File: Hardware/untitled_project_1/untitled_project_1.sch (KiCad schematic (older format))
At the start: 1 part

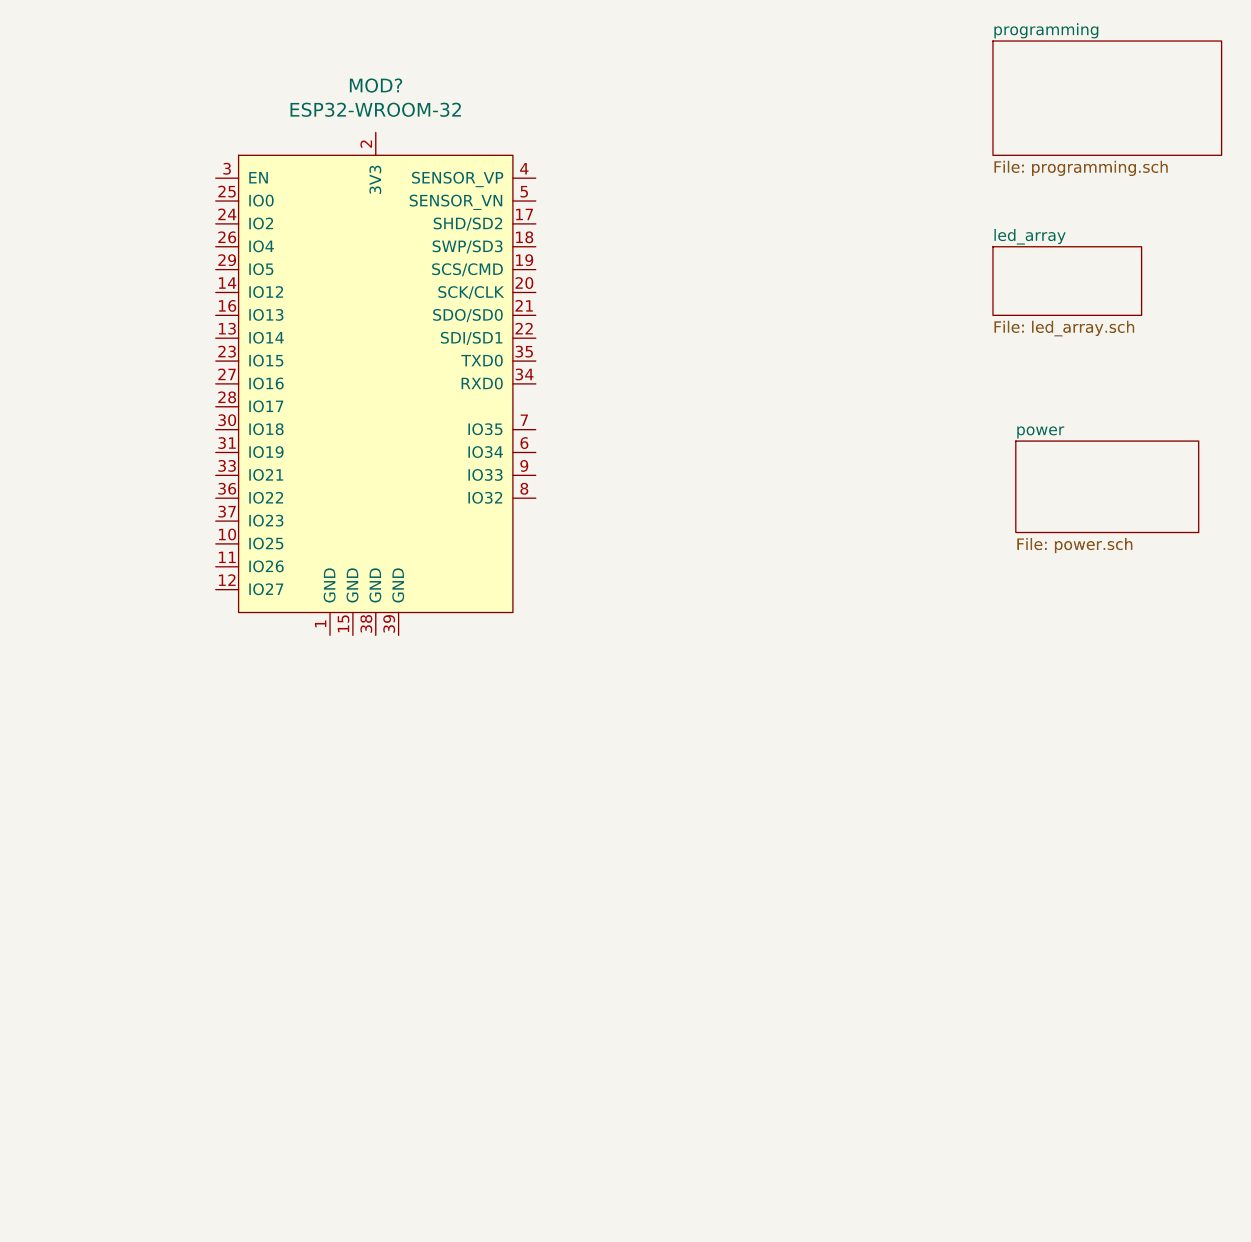
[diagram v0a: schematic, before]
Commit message: add power and programming schematics
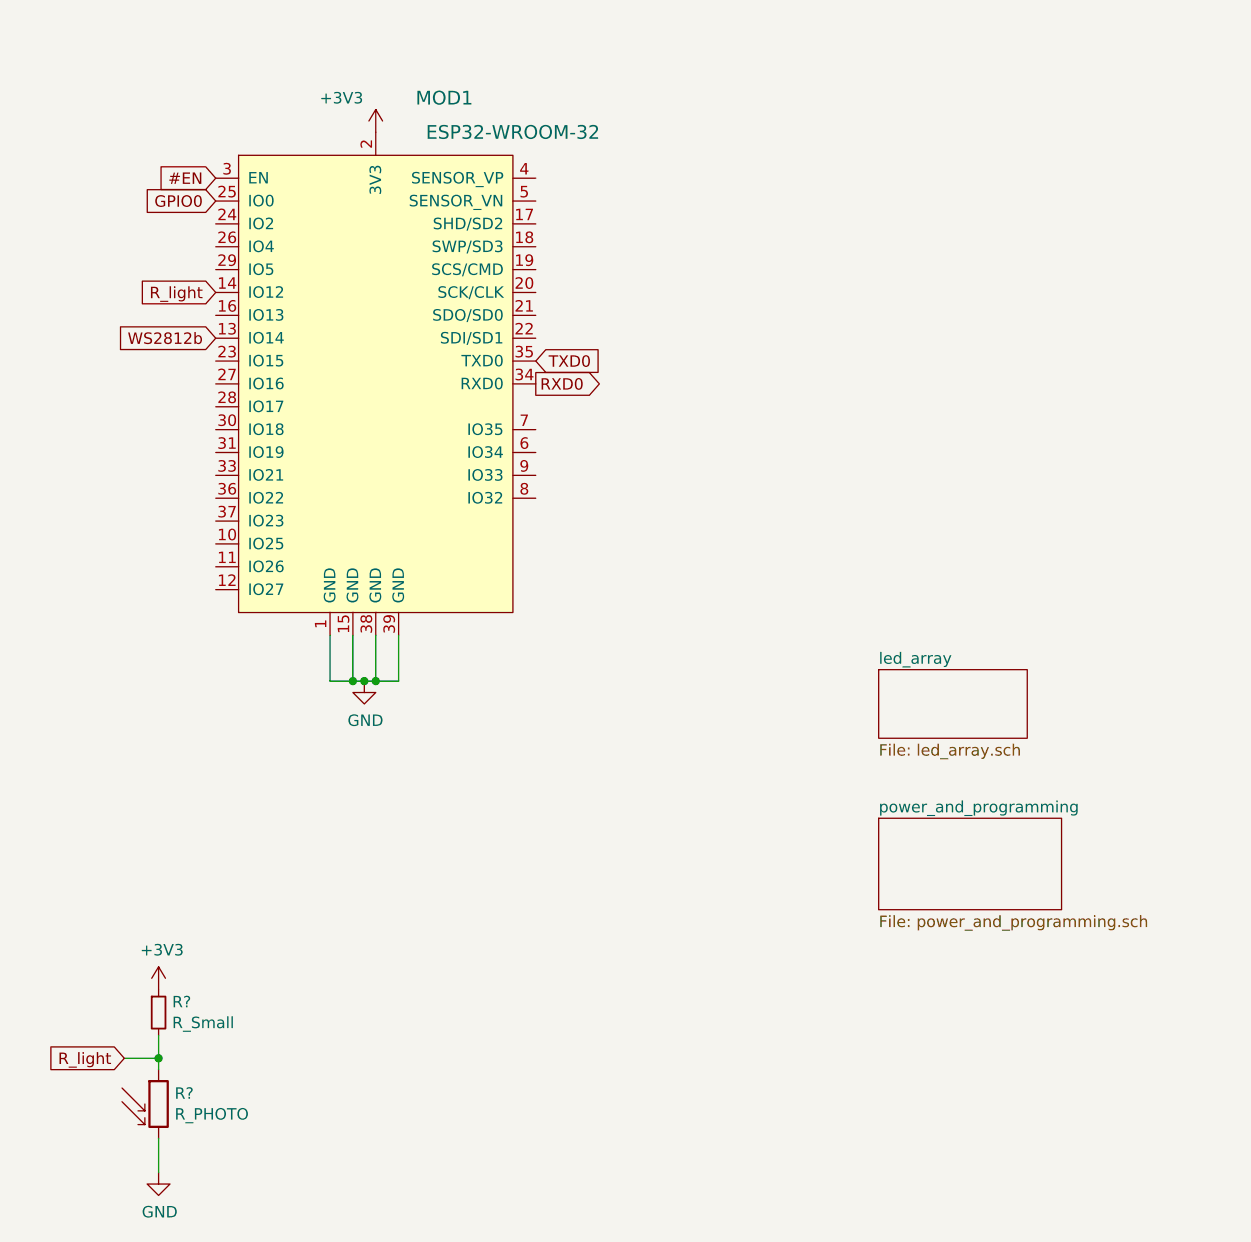
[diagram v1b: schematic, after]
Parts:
- added R?: R_PHOTO, symbol Device:R_PHOTO
- added R?: R_Small, symbol Device:R_Small
- gave numbers to parts that had none: 1
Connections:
- net GND: now reaches MOD1.1 (GND)
- net GND: now also MOD1.15 (GND), MOD1.38 (GND), MOD1.39 (GND), R?.2
- net WS2812b: now reaches MOD1.13 (IO14)
- net R_light: now reaches MOD1.14 (IO12)
- net R_light: now also R?.1, R?.2
- net +3V3: now reaches MOD1.2 (3V3)
- net +3V3: now also R?.1
- net GPIO0: now reaches MOD1.25 (IO0)
- net #EN: now reaches MOD1.3 (EN)
- net RXD0: now reaches MOD1.34 (RXD0)
- net TXD0: now reaches MOD1.35 (TXD0)

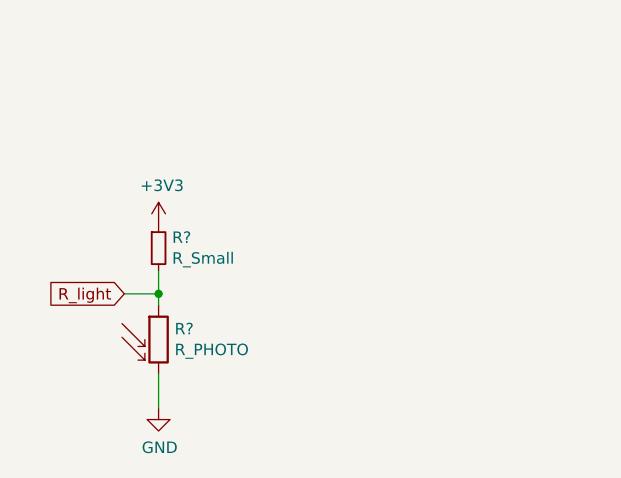
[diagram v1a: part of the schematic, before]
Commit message: add footprints to szymbols:
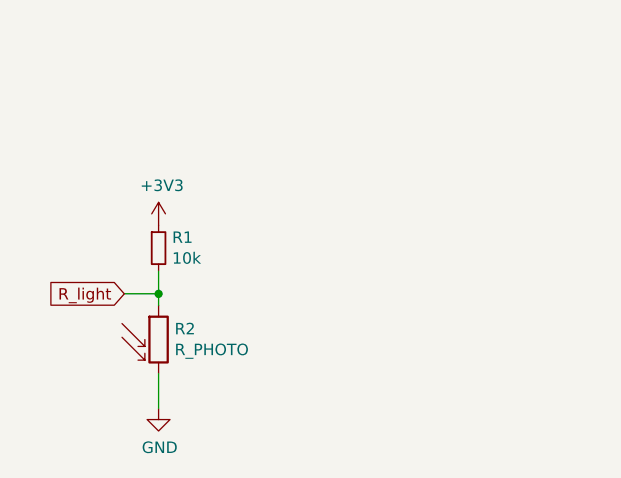
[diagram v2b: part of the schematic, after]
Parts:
- MOD1: footprint digikey-footprints:ESP32-WROOM-32D -> digikey-symbolsold:ESP32-WROOM-32D
- R1: renamed from R?; value R_Small -> 10k; footprint (none) -> Resistor_SMD:R_1210_3225Metric_Pad1.42x2.65mm_HandSolder
- R2: renamed from R?; footprint (none) -> Resistor_SMD:R_1210_3225Metric_Pad1.42x2.65mm_HandSolder
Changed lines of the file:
@@
 F 0 "MOD1" H 3100 1850 60  0000 C CNN
 F 1 "ESP32-WROOM-32" H 3400 1700 60  0000 C CNN
-F 2 "digikey-footprints:ESP32-WROOM-32D" H 2800 1800 60  0001 L CNN
+F 2 "digikey-symbolsold:ESP32-WROOM-32D" H 2800 1800 60  0001 L CNN
 F 3 "https://www.espressif.com/sites/default/files/documentation/esp32-wroom-32_datasheet_en.pdf" H 2800 1900 60  0001 L CNN
 F 4 "1904-1010-1-ND" H 2800 2000 60  0001 L CNN "Digi-Key_PN"
@@
 WS2812b
 $Comp
-L Device:R_PHOTO R?
+L Device:R_PHOTO R2
 U 1 1 5F09AEAE
 P 1850 5750
-F 0 "R?" H 1920 5796 50  0000 L CNN
+F 0 "R2" H 1920 5796 50  0000 L CNN
 F 1 "R_PHOTO" H 1920 5705 50  0000 L CNN
-F 2 "" V 1900 5500 50  0001 L CNN
+F 2 "Resistor_SMD:R_1210_3225Metric_Pad1.42x2.65mm_HandSolder" V 1900 5500 50  0001 L CNN
 F 3 "~" H 1850 5700 50  0001 C CNN
 	1    1850 5750
@@
 $EndComp
 $Comp
-L Device:R_Small R?
+L Device:R_Small R1
 U 1 1 5F09BCA6
 P 1850 5350
-F 0 "R?" H 1909 5396 50  0000 L CNN
-F 1 "R_Small" H 1909 5305 50  0000 L CNN
-F 2 "" H 1850 5350 50  0001 C CNN
+F 0 "R1" H 1909 5396 50  0000 L CNN
+F 1 "10k" H 1909 5305 50  0000 L CNN
+F 2 "Resistor_SMD:R_1210_3225Metric_Pad1.42x2.65mm_HandSolder" H 1850 5350 50  0001 C CNN
 F 3 "~" H 1850 5350 50  0001 C CNN
 	1    1850 5350
@@
 $EndComp
 $Comp
-L power:+3V3 #PWR?
+L power:+3V3 #PWR0101
 U 1 1 5F09C4D8
 P 1850 5250
-F 0 "#PWR?" H 1850 5100 50  0001 C CNN
+F 0 "#PWR0101" H 1850 5100 50  0001 C CNN
 F 1 "+3V3" H 1865 5423 50  0000 C CNN
 F 2 "" H 1850 5250 50  0001 C CNN
@@
 $EndComp
 $Comp
-L power:GND #PWR?
+L power:GND #PWR0102
 U 1 1 5F09CB5B
 P 1850 6050
-F 0 "#PWR?" H 1850 5800 50  0001 C CNN
+F 0 "#PWR0102" H 1850 5800 50  0001 C CNN
 F 1 "GND" H 1855 5877 50  0000 C CNN
 F 2 "" H 1850 6050 50  0001 C CNN
@@
 R_light
 $Comp
-L power:+3V3 #PWR?
+L power:+3V3 #PWR0103
 U 1 1 5F09F643
 P 2800 1500
-F 0 "#PWR?" H 2800 1350 50  0001 C CNN
+F 0 "#PWR0103" H 2800 1350 50  0001 C CNN
 F 1 "+3V3" H 2650 1650 50  0000 C CNN
 F 2 "" H 2800 1500 50  0001 C CNN
@@
 $EndComp
 $Comp
-L power:GND #PWR?
+L power:GND #PWR0104
 U 1 1 5F0A017A
 P 2750 3900
-F 0 "#PWR?" H 2750 3650 50  0001 C CNN
+F 0 "#PWR0104" H 2750 3650 50  0001 C CNN
 F 1 "GND" H 2755 3727 50  0000 C CNN
 F 2 "" H 2750 3900 50  0001 C CNN
